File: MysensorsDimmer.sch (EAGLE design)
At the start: 58 parts, among them IC1 7805DT, IC2 AT25DF512C-SSHN-B, IC3 ATSHA204A, J1 22-27-2021-02, J2 22-27-2021-02, J3 22-27-2021-02, J4 22-27-2021-02, J5 22-27-2021-02, M1 WIRELESS-NRF24L01, Q1 IRF530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

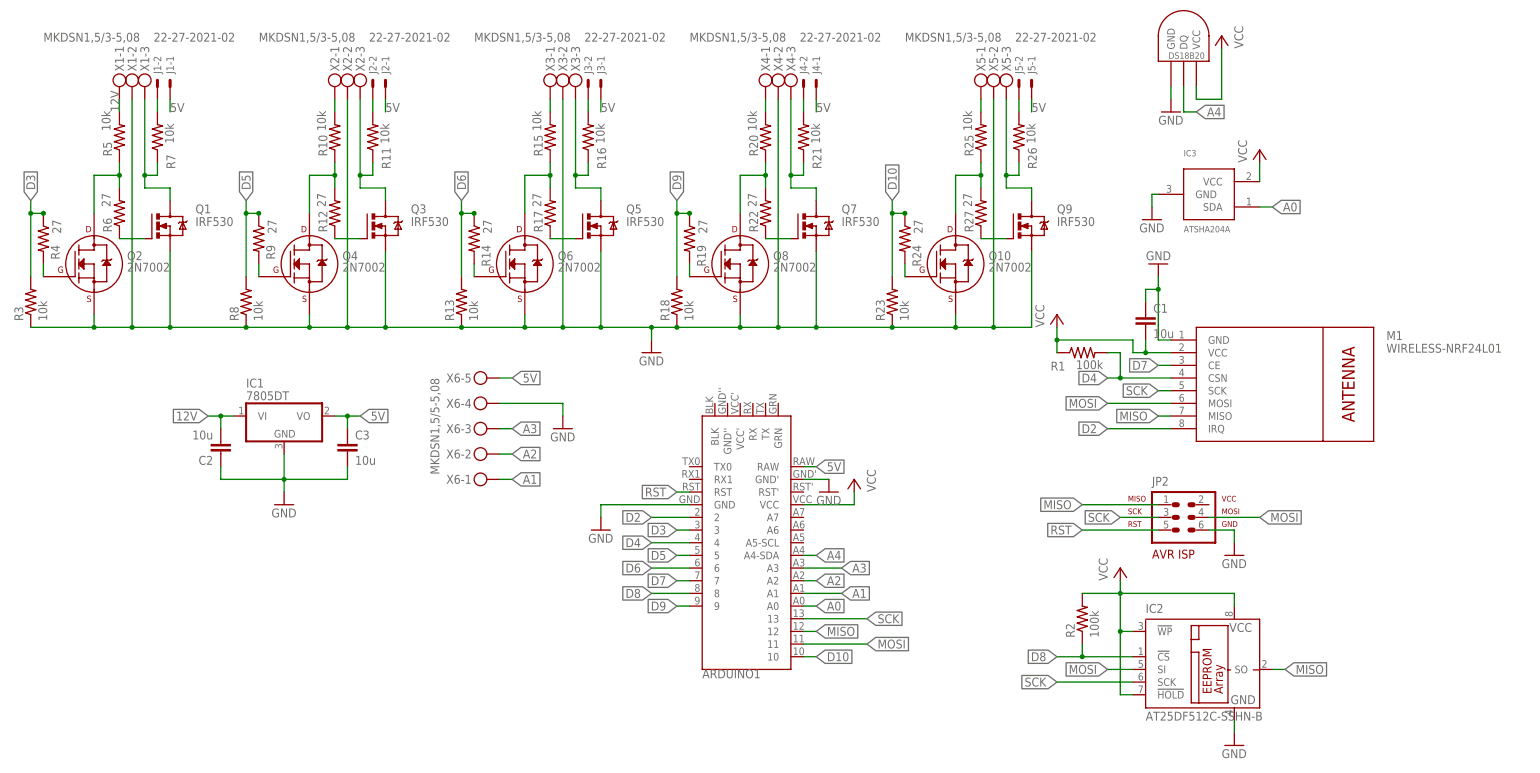
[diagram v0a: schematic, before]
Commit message: corrected descriptions, names, etc.
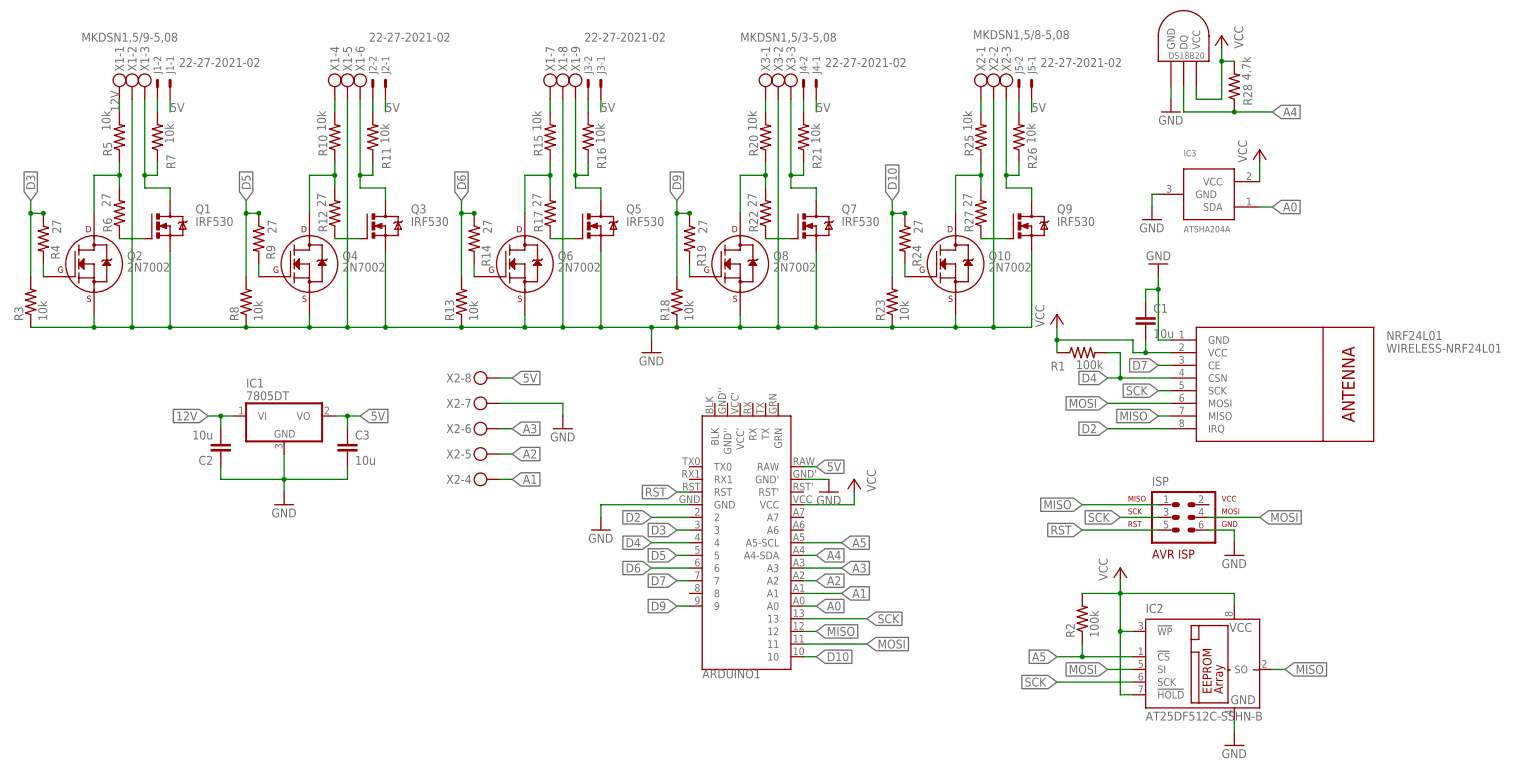
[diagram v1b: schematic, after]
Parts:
- removed X4, X5: MKDSN1,5/3-5,08, con-phoenix-508:MKDSN1,5/3-5,08
- removed X6: MKDSN1,5/5-5,08, con-phoenix-508:MKDSN1,5/5-5,08
- added R28: 4.7k, SparkFun-Passives:RESISTOR0603-RES
- X1: value MKDSN1,5/3-5,08 -> MKDSN1,5/9-5,08; device con-phoenix-508:MKDSN1,5/3-5,08 -> con-phoenix-508:MKDSN1,5/9-5,08
- X2: value MKDSN1,5/3-5,08 -> MKDSN1,5/8-5,08; device con-phoenix-508:MKDSN1,5/3-5,08 -> con-phoenix-508:MKDSN1,5/8-5,08
- renumbered JP2 to ISP, M1 to NRF24L01, U$1 to IC4
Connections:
- removed net D8: ARDUINO1.8, IC2.!CS, R2.1
- new net A5: ARDUINO1.A5-SCL, IC2.!CS, R2.1
- net 5V: now also X2-8.KL; no longer X6-5.KL
- net A1: now also X2-4.KL; no longer X6-1.KL
- net A2: now also X2-5.KL; no longer X6-2.KL
- net A3: now also X2-6.KL; no longer X6-3.KL
- net A4: now also R28.1
- net GND: now also X1-5.KL, X1-8.KL, X2-7.KL; no longer X4-2.KL, X5-2.KL, X6-4.KL
- net N$1: now also X1-6.KL; no longer X2-3.KL
- net N$10: now also X1-9.KL; no longer X3-3.KL
- net N$15: now also X3-3.KL; no longer X4-3.KL
- net N$20: now also X2-3.KL; no longer X5-3.KL
- net N$26: now also X1-4.KL; no longer X2-1.KL
- net N$27: now also X1-7.KL; no longer X3-1.KL
- net N$28: now also X3-1.KL; no longer X4-1.KL
- net N$29: now also X2-1.KL; no longer X5-1.KL
- net VCC: now also R28.2
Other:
- moved on the sheet: X2-1, X2-2, X2-3, X3-1, X3-2, X3-3

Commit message: modifications after v1.0 version (see changelog.txt)
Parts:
- C2: device SparkFun-Passives:CAP0603-CAP -> SparkFun-Passives:CAP1206
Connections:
- new net D8: ARDUINO1.8, IC2.!CS, R2.1
- net A5: no longer IC2.!CS, R2.1
- net VCC: now also ISP.2
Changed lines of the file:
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@@
 <part name="R7" library="SparkFun-Passives" deviceset="RESISTOR" device="0603-RES" value="10k"/>
 <part name="IC1" library="linear" deviceset="78*" device="DT" technology="05"/>
-<part name="C2" library="SparkFun-Passives" deviceset="CAP" device="0603-CAP" value="10u"/>
+<part name="C2" library="SparkFun-Passives" deviceset="CAP" device="1206" value="10u"/>
 <part name="C3" library="SparkFun-Passives" deviceset="CAP" device="0603-CAP" value="10u"/>
 <part name="GND5" library="supply1" deviceset="GND" device=""/>
@@
 <part name="R28" library="SparkFun-Passives" deviceset="RESISTOR" device="0603-RES" value="4.7k"/>
 <part name="IC4" library="Ava" deviceset="DS1820" device=""/>
+<part name="P+6" library="supply1" deviceset="VCC" device=""/>
 </parts>
 <sheets>
@@
 </instance>
 <instance part="IC4" gate="G$1" x="167.64" y="152.4"/>
+<instance part="P+6" gate="VCC" x="177.8" y="71.12"/>
 </instances>
 <busses>
@@
 <pinref part="P+5" gate="VCC" pin="VCC"/>
 </segment>
+<segment>
+<pinref part="ISP" gate="G$1" pin="2"/>
+<wire x1="172.72" y1="63.5" x2="177.8" y2="63.5" width="0.1524" layer="91"/>
+<pinref part="P+6" gate="VCC" pin="VCC"/>
+<wire x1="177.8" y1="63.5" x2="177.8" y2="68.58" width="0.1524" layer="91"/>
+</segment>
 </net>
 <net name="A5" class="0">
@@
 <label x="99.06" y="55.88" size="1.778" layer="95" xref="yes"/>
 </segment>
-<segment>
+</net>
+<net name="D8" class="0">
+<segment>
+<pinref part="ARDUINO1" gate="G$1" pin="8"/>
+<wire x1="68.58" y1="45.72" x2="60.96" y2="45.72" width="0.1524" layer="91"/>
+<label x="60.96" y="45.72" size="1.778" layer="95" rot="R180" xref="yes"/>
+</segment>
+<segment>

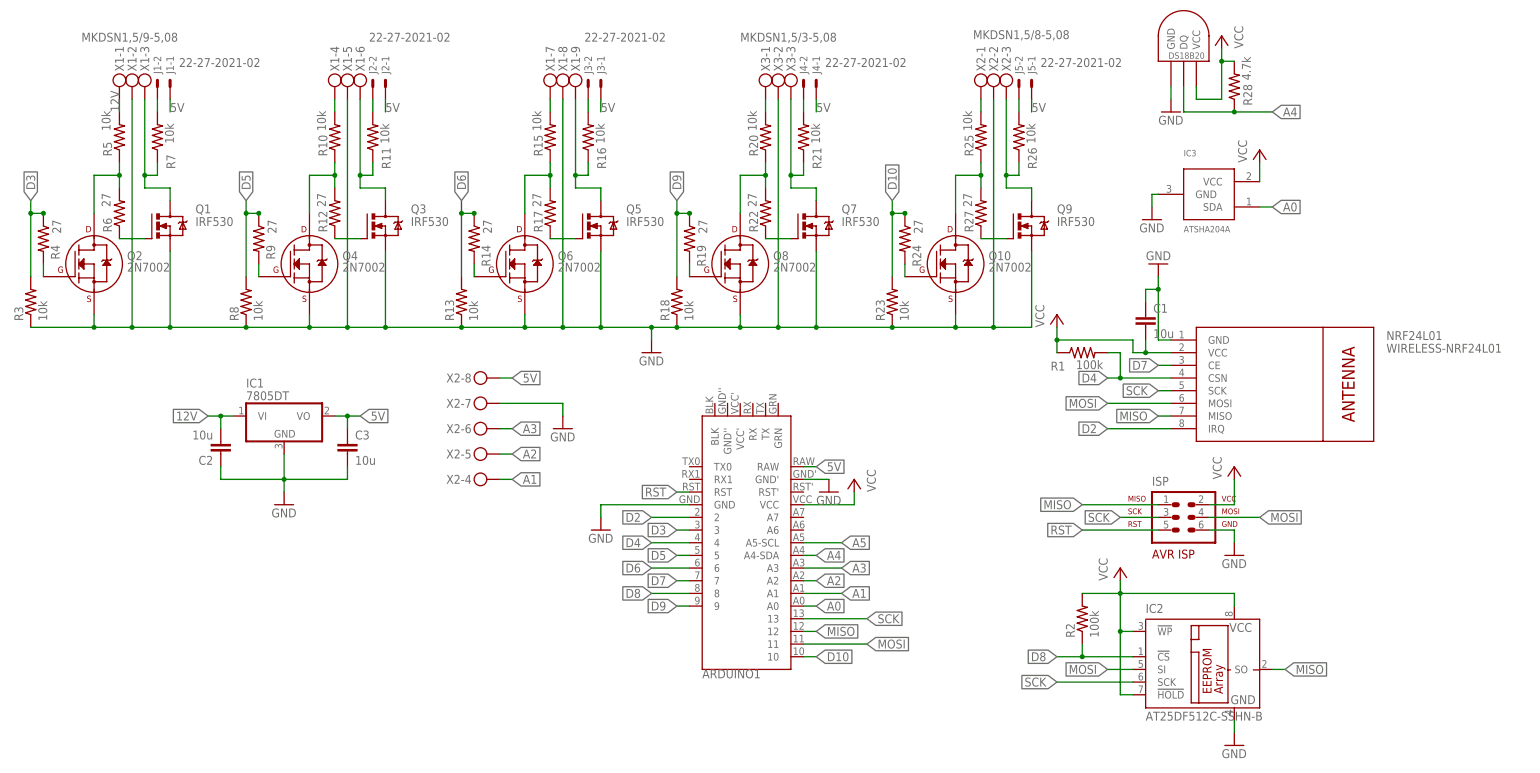
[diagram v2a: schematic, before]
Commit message: add i2c connection for apds 9930
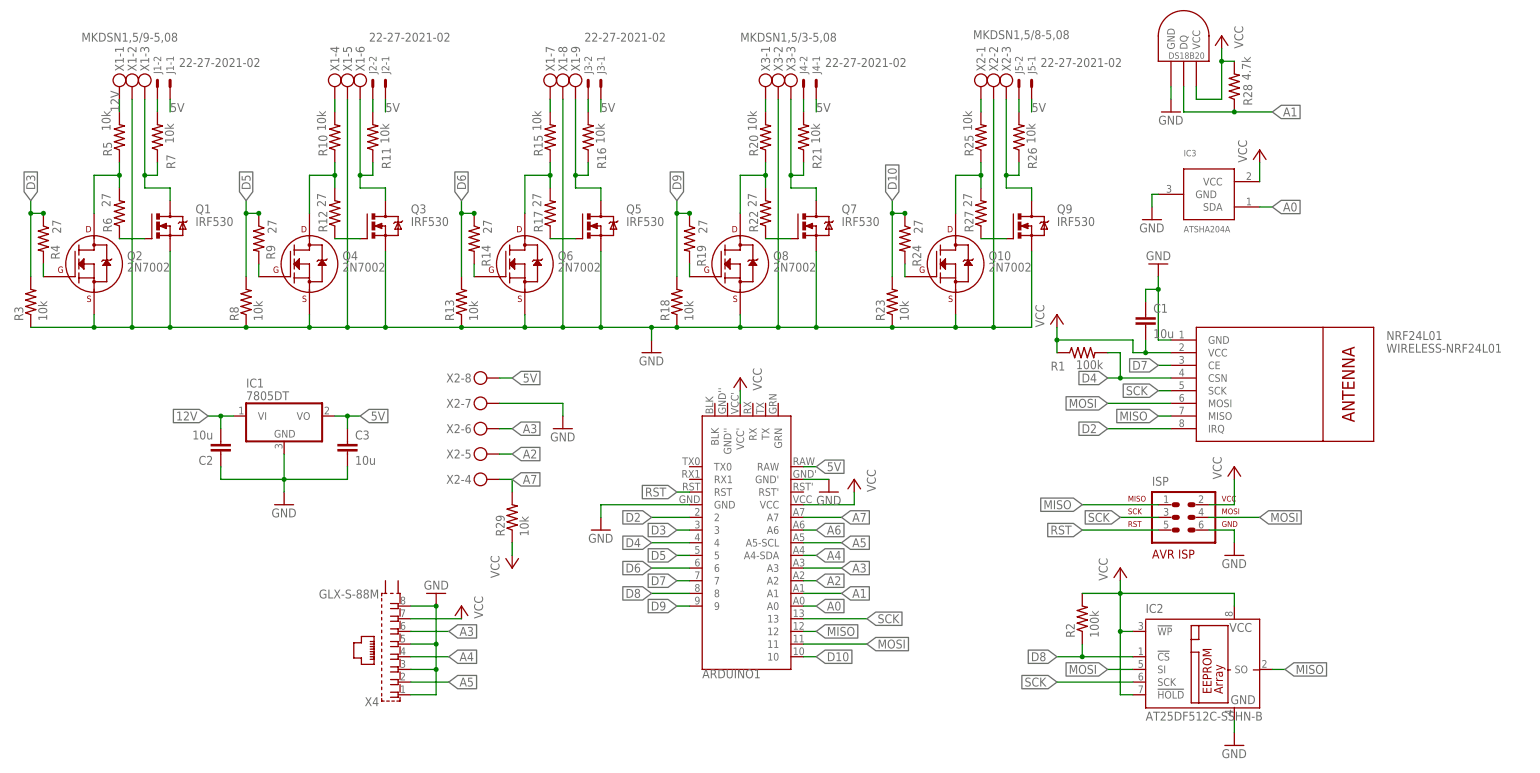
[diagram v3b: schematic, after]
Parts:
- added R29: 10k, SparkFun-Passives:RESISTOR0603-RES
- added X4: GLX-S-88M, con-kycon:GLX-S-88M
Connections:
- new net A6: ARDUINO1.A6
- new net A7: ARDUINO1.A7, R29.2, X2-4.KL
- net A1: now also IC4.DQ, R28.1; no longer X2-4.KL
- net A3: now also X4.6
- net A4: now also X4.4; no longer IC4.DQ, R28.1
- net A5: now also X4.2
- net GND: now also X4.1, X4.3, X4.5, X4.8
- net VCC: now also ARDUINO1.VCC', R29.1, X4.7
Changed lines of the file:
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@@
 <part name="IC4" library="Ava" deviceset="DS1820" device=""/>
 <part name="P+6" library="supply1" deviceset="VCC" device=""/>
+<part name="X4" library="con-kycon" deviceset="GLX-S-88M" device=""/>
+<part name="P+7" library="supply1" deviceset="VCC" device=""/>
+<part name="GND7" library="supply1" deviceset="GND" device=""/>
+<part name="P+8" library="supply1" deviceset="VCC" device=""/>
+<part name="R29" library="SparkFun-Passives" deviceset="RESISTOR" device="0603-RES" value="10k"/>
+<part name="P+9" library="supply1" deviceset="VCC" device=""/>
 </parts>
 <sheets>
@@
 <instance part="IC4" gate="G$1" x="167.64" y="152.4"/>
 <instance part="P+6" gate="VCC" x="177.8" y="71.12"/>
+<instance part="X4" gate="G$1" x="10.16" y="35.56" rot="R180"/>
+<instance part="P+7" gate="VCC" x="22.86" y="43.18" rot="MR0"/>
+<instance part="GND7" gate="1" x="17.78" y="45.72" rot="R180"/>
+<instance part="P+8" gate="VCC" x="78.74" y="88.9" rot="MR0"/>
+<instance part="R29" gate="G$1" x="33.02" y="60.96" rot="R90"/>
+<instance part="P+9" gate="VCC" x="33.02" y="50.8" rot="MR180"/>
 </instances>
 <busses>
@@
 <pinref part="IC4" gate="G$1" pin="GND"/>
 </segment>
+<segment>
+<pinref part="X4" gate="G$1" pin="8"/>
+<wire x1="12.7" y1="43.18" x2="17.78" y2="43.18" width="0.1524" layer="91"/>
+<pinref part="GND7" gate="1" pin="GND"/>
+<pinref part="X4" gate="G$1" pin="5"/>
+<wire x1="12.7" y1="35.56" x2="17.78" y2="35.56" width="0.1524" layer="91"/>
+<wire x1="17.78" y1="35.56" x2="17.78" y2="43.18" width="0.1524" layer="91"/>
+<pinref part="X4" gate="G$1" pin="3"/>
+<wire x1="12.7" y1="30.48" x2="17.78" y2="30.48" width="0.1524" layer="91"/>
+<wire x1="17.78" y1="30.48" x2="17.78" y2="35.56" width="0.1524" layer="91"/>
+<pinref part="X4" gate="G$1" pin="1"/>
+<wire x1="12.7" y1="25.4" x2="17.78" y2="25.4" width="0.1524" layer="91"/>
+<wire x1="17.78" y1="25.4" x2="17.78" y2="30.48" width="0.1524" layer="91"/>
+<junction x="17.78" y="30.48"/>
+<junction x="17.78" y="35.56"/>
+<junction x="17.78" y="43.18"/>
+</segment>
 </net>
 <net name="D4" class="0">
@@
 <label x="33.02" y="78.74" size="1.778" layer="95" xref="yes"/>
 <pinref part="X2" gate="-6" pin="KL"/>
+</segment>
+<segment>
+<pinref part="X4" gate="G$1" pin="6"/>
+<wire x1="12.7" y1="38.1" x2="20.32" y2="38.1" width="0.1524" layer="91"/>
+<label x="20.32" y="38.1" size="1.778" layer="95" xref="yes"/>
 </segment>
 </net>
@@
 </segment>
 <segment>
-<label x="33.02" y="68.58" size="1.778" layer="95" xref="yes"/>
-<wire x1="30.48" y1="68.58" x2="33.02" y2="68.58" width="0.1524" layer="91"/>
-<pinref part="X2" gate="-4" pin="KL"/>
-</segment>
-</net>
-<net name="A2" class="0">
-<segment>
-<wire x1="93.98" y1="48.26" x2="91.44" y2="48.26" width="0.1524" layer="91"/>
-<label x="93.98" y="48.26" size="1.778" layer="95" xref="yes"/>
-<pinref part="ARDUINO1" gate="G$1" pin="A2"/>
-</segment>
-<segment>
-<label x="33.02" y="73.66" size="1.778" layer="95" xref="yes"/>
-<wire x1="30.48" y1="73.66" x2="33.02" y2="73.66" width="0.1524" layer="91"/>
-<pinref part="X2" gate="-5" pin="KL"/>
-</segment>
-</net>
-<net name="A4" class="0">
-<segment>
-<pinref part="ARDUINO1" gate="G$1" pin="A4-SDA"/>
-<wire x1="91.44" y1="53.34" x2="93.98" y2="53.34" width="0.1524" layer="91"/>
-<label x="93.98" y="53.34" size="1.778" layer="95" xref="yes"/>
-</segment>
-<segment>
 <wire x1="167.64" y1="147.32" x2="167.64" y2="142.24" width="0.1524" layer="91"/>
 <wire x1="167.64" y1="142.24" x2="177.8" y2="142.24" width="0.1524" layer="91"/>
@@
 <junction x="177.8" y="142.24"/>
 <pinref part="IC4" gate="G$1" pin="DQ"/>
+</segment>
+</net>
+<net name="A2" class="0">
+<segment>
+<wire x1="93.98" y1="48.26" x2="91.44" y2="48.26" width="0.1524" layer="91"/>
+<label x="93.98" y="48.26" size="1.778" layer="95" xref="yes"/>
+<pinref part="ARDUINO1" gate="G$1" pin="A2"/>
+</segment>
+<segment>
+<label x="33.02" y="73.66" size="1.778" layer="95" xref="yes"/>
+<wire x1="30.48" y1="73.66" x2="33.02" y2="73.66" width="0.1524" layer="91"/>
+<pinref part="X2" gate="-5" pin="KL"/>
+</segment>
+</net>
+<net name="A4" class="0">
+<segment>
+<pinref part="ARDUINO1" gate="G$1" pin="A4-SDA"/>
+<wire x1="91.44" y1="53.34" x2="93.98" y2="53.34" width="0.1524" layer="91"/>
+<label x="93.98" y="53.34" size="1.778" layer="95" xref="yes"/>
+</segment>
+<segment>
+<pinref part="X4" gate="G$1" pin="4"/>
+<wire x1="12.7" y1="33.02" x2="20.32" y2="33.02" width="0.1524" layer="91"/>
+<label x="20.32" y="33.02" size="1.778" layer="95" xref="yes"/>
 </segment>
 </net>
@@
 <wire x1="177.8" y1="63.5" x2="177.8" y2="68.58" width="0.1524" layer="91"/>
 </segment>
+<segment>
+<pinref part="X4" gate="G$1" pin="7"/>
+<wire x1="12.7" y1="40.64" x2="22.86" y2="40.64" width="0.1524" layer="91"/>
+<pinref part="P+7" gate="VCC" pin="VCC"/>
+</segment>
+<segment>
+<pinref part="ARDUINO1" gate="G$1" pin="VCC'"/>
+<wire x1="78.74" y1="83.82" x2="78.74" y2="86.36" width="0.1524" layer="91"/>
+<pinref part="P+8" gate="VCC" pin="VCC"/>
+</segment>
+<segment>
+<pinref part="R29" gate="G$1" pin="1"/>
+<pinref part="P+9" gate="VCC" pin="VCC"/>
+<wire x1="33.02" y1="53.34" x2="33.02" y2="55.88" width="0.1524" layer="91"/>
+</segment>
 </net>
 <net name="A5" class="0">
@@
 <wire x1="91.44" y1="55.88" x2="99.06" y2="55.88" width="0.1524" layer="91"/>
 <label x="99.06" y="55.88" size="1.778" layer="95" xref="yes"/>
+</segment>
+<segment>
+<pinref part="X4" gate="G$1" pin="2"/>
+<wire x1="12.7" y1="27.94" x2="20.32" y2="27.94" width="0.1524" layer="91"/>
+<label x="20.32" y="27.94" size="1.778" layer="95" xref="yes"/>
 </segment>
 </net>
@@
 </segment>
 </net>
+<net name="A6" class="0">
+<segment>
+<pinref part="ARDUINO1" gate="G$1" pin="A6"/>
+<wire x1="91.44" y1="58.42" x2="93.98" y2="58.42" width="0.1524" layer="91"/>
+<label x="93.98" y="58.42" size="1.778" layer="95" xref="yes"/>
+</segment>
+</net>
+<net name="A7" class="0">
+<segment>
+<pinref part="ARDUINO1" gate="G$1" pin="A7"/>
+<wire x1="91.44" y1="60.96" x2="99.06" y2="60.96" width="0.1524" layer="91"/>
+<label x="99.06" y="60.96" size="1.778" layer="95" xref="yes"/>
+</segment>
+<segment>
+<label x="33.02" y="68.58" size="1.778" layer="95" xref="yes"/>
+<wire x1="30.48" y1="68.58" x2="33.02" y2="68.58" width="0.1524" layer="91"/>
+<pinref part="X2" gate="-4" pin="KL"/>
+<pinref part="R29" gate="G$1" pin="2"/>
+<wire x1="33.02" y1="66.04" x2="33.02" y2="68.58" width="0.1524" layer="91"/>
+</segment>
+</net>
